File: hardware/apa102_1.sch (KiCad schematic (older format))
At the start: 77 parts

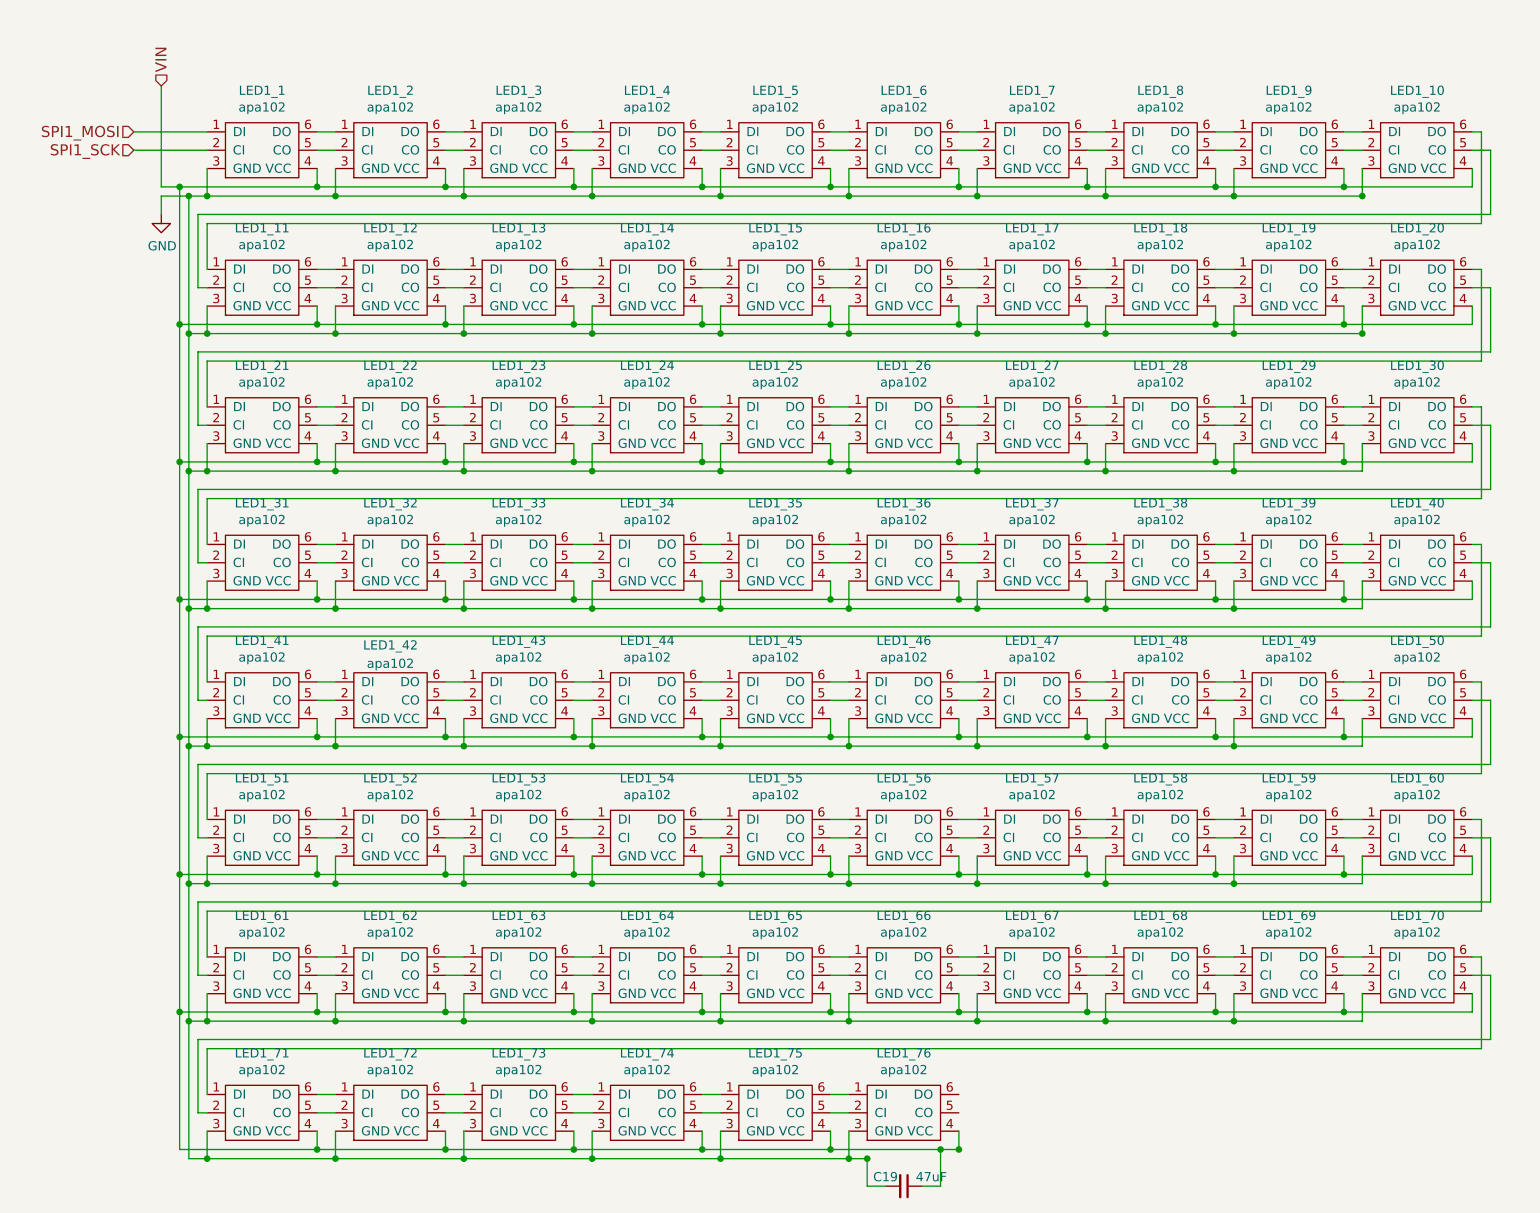
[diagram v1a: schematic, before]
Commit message: Removed 72 LEDs
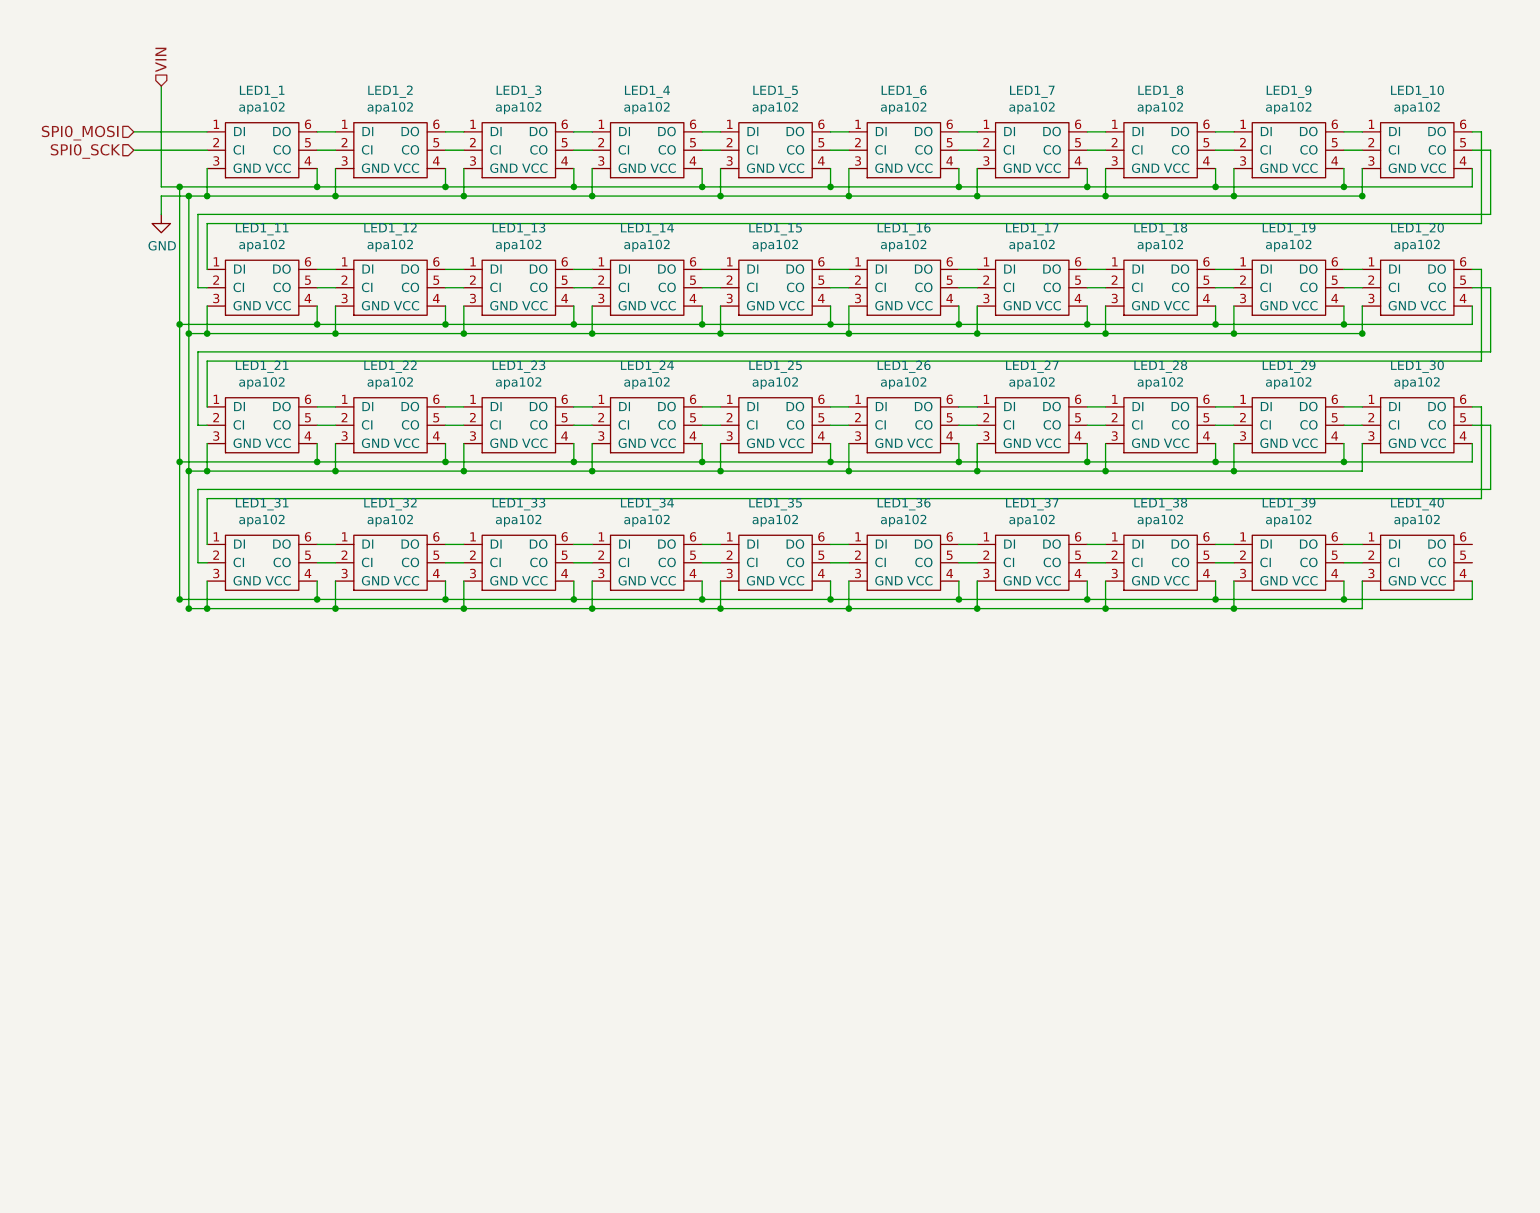
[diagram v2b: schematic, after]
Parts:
- removed C19: 47uF, Capacitors_SMD:C_0805, symbol C_Small
- removed LED1_41, LED1_42, LED1_43, LED1_44, LED1_45, LED1_46, LED1_47, LED1_48, LED1_49, LED1_50, LED1_51, LED1_52, LED1_53, LED1_54, LED1_55, LED1_56, LED1_57, LED1_58, LED1_59, LED1_60, LED1_61, LED1_62, LED1_63, LED1_64, LED1_65, LED1_66, LED1_67, LED1_68, LED1_69, LED1_70, LED1_71, LED1_72, LED1_73, LED1_74, LED1_75, LED1_76: apa102, apa102:apa102, symbol apa102
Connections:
- net SPI1_MOSI renamed SPI0_MOSI
- net SPI1_SCK renamed SPI0_SCK

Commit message: Switched to fat small design
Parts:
- LED1_1, LED1_10, LED1_11, LED1_12, LED1_13, LED1_14, LED1_15, LED1_16, LED1_17, LED1_18, LED1_19, LED1_2, LED1_20, LED1_21, LED1_22, LED1_23, LED1_24, LED1_25, LED1_26, LED1_27, LED1_28, LED1_29, LED1_3, LED1_30, LED1_31, LED1_32, LED1_33, LED1_34, LED1_35, LED1_36, LED1_37, LED1_38, LED1_39, LED1_4, LED1_40, LED1_5, LED1_6, LED1_7, LED1_8, LED1_9: symbol apa102 -> APA102

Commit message: Fixed APA102 bank 1 SPI trace names
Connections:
- net labels added: SPI1_MOSI, SPI1_SCK
- net labels removed: SPI0_MOSI, SPI0_SCK
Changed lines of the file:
@@
 $Descr A4 11693 8268
 encoding utf-8
-Sheet 4 6
+Sheet 5 6
 Title ""
 Date ""
@@
 $EndComp
 Text HLabel 2000 1100 0    60   Input ~ 0
-SPI0_MOSI
+SPI1_MOSI
 Text HLabel 2000 1200 0    60   Input ~ 0
-SPI0_SCK
+SPI1_SCK
 $Comp
 L GND #PWR015
